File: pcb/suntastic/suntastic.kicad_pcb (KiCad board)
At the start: 2 copper layers, 105 parts, among them J1 Screw_Terminal_01x02, J2 Pololu U1V10F5, J3 Supercap IN, J4 FBB04004-F40S1003K6M, J5 Vin_TO_buck_boost, J6 Vout_FROM_buck_boost, J7 Conn_01x04_Pin, J8 Conn_01x04_Pin, J9 Conn_01x08_Pin, SW1 EVP-BF6C1A000, U1 TLV3691IDCKR, U2 REF35102QDBVR, U3 REF35409QDBVR, U4 TLV3691IDCKR, U5 TC7WH02FU_LJCT, U6 TPS22917DBV, U7 TPL5010, U8 XC6220B331MR

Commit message: Rework watchdog
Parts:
- removed TP10: IO1, TestPoint:TestPoint_Pad_D1.5mm
- removed TP11: IO6, TestPoint:TestPoint_Pad_D1.5mm
- removed TP12: IO8, TestPoint:TestPoint_Pad_D1.5mm
- removed TP13: IO7, TestPoint:TestPoint_Pad_D1.5mm
- removed TP14: VDD_nRF, TestPoint:TestPoint_Pad_D1.5mm
- removed TP6: IO4, TestPoint:TestPoint_Pad_D1.5mm
- removed TP7: IO2, TestPoint:TestPoint_Pad_D1.5mm
- removed TP8: IO5, TestPoint:TestPoint_Pad_D1.5mm
- removed TP9: IO3, TestPoint:TestPoint_Pad_D1.5mm
- added C21: 1uF, Capacitor_SMD:C_0603_1608Metric_Pad1.08x0.95mm_HandSolder, F.Cu at (56.7, 77.5)
- added C24: 0.1uF, Capacitor_SMD:C_0603_1608Metric_Pad1.08x0.95mm_HandSolder, F.Cu at (72.1, 71.4)
- added C25: 1uF, Capacitor_SMD:CP_Elec_4x4.5, F.Cu at (68.3, 73.7)
- added JP28: SolderJumper_2_Open, Jumper:SolderJumper-2_P1.3mm_Open_RoundedPad1.0x1.5mm, F.Cu at (59.3, 75.3)
- added R4: R, Resistor_SMD:R_0603_1608Metric_Pad0.98x0.95mm_HandSolder, F.Cu at (59.3, 83.5)
- added R7: R, Resistor_SMD:R_0603_1608Metric_Pad0.98x0.95mm_HandSolder, F.Cu at (59.3, 82.0)
- added R8: R, Resistor_SMD:R_0603_1608Metric_Pad0.98x0.95mm_HandSolder, F.Cu at (56.7, 81.0)
- added U10: TC7WH08FK_LJCT, Package_SO:TSSOP-8_3x3mm_P0.65mm, F.Cu at (74.9, 73.3)
- added U9: TPS22917DBV, Package_TO_SOT_SMD:SOT-23-6, F.Cu at (59.3, 79.0)
- JP27: value Jumper_2_Open -> SolderJumper_2_Open
- TP5: footprint TestPoint:TestPoint_Pad_D1.5mm -> TestPoint:TestPoint_Pad_D1.0mm
- U5: footprint Package_SO:Zetex_SM8 -> Package_SO:TSSOP-8_3x3mm_P0.65mm
- moved RV1 139.1 mm to (47.3, 72.6), turned to 180 degrees
- moved JP22 136.0 mm to (54.1, 79.7), turned to 180 degrees
- moved U7 134.6 mm to (53.7, 82.8)
- moved SW1 133.2 mm to (47.9, 80.0), turned to -90 degrees
- moved JP27 116.4 mm to (74.0, 83.0), turned to -90 degrees
- moved J1 85.6 mm to (130.0, 96.0)
- moved J2 85.4 mm to (141.7, 89.8)
- moved J9 32.4 mm to (174.6, 77.8), turned to 180 degrees
- moved JP20 28.9 mm to (144.6, 73.3), turned to -90 degrees
- moved JP25 28.5 mm to (149.6, 57.8)
- moved J8 27.7 mm to (150.8, 70.7)
- moved TP3 27.6 mm to (71.1, 83.9), turned to -90 degrees
- moved C18 22.2 mm to (166.3, 76.8)
- moved C17 22.0 mm to (159.8, 76.8), turned to 180 degrees
- moved TP4 21.7 mm to (163.1, 77.2)
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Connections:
- J9 pad 2: /WisBlock Core Module - RAK4631/IO2 -> /WisBlock Core Module - RAK4631/IO5
- J9 pad 4: /WisBlock Core Module - RAK4631/IO4 -> /WisBlock Core Module - RAK4631/IO6
- J9 pad 5: /WisBlock Core Module - RAK4631/IO5 -> /WisBlock Core Module - RAK4631/IO4
- J9 pad 6: /WisBlock Core Module - RAK4631/IO6 -> /WisBlock Core Module - RAK4631/IO2
- JP22 pad 1: 3.3V -> V_boost_uvlo
- JP27 pad 1: /Watchdog timer/RST_SIGNAL -> Net-(JP27-A)
- JP27 pad 2: nRF_RESET -> Net-(J1-Pin_1)
- SW1 pad 2: 3.3V -> V_boost_uvlo
- U6 pad 3: Net-(JP15-B) -> Net-(U10-OUT_2)
- U6 pad 5: unconnected-(U6-QOD-Pad5) -> Net-(JP27-A)
- U7 pad 4: unconnected-(U7-DONE-Pad4) -> Net-(JP28-A)
- U7 pad 5: unconnected-(U7-WAKE-Pad5) -> Net-(U7-WAKE)
- U7 pad 6: /Watchdog timer/RST_SIGNAL -> RST_SIGNAL
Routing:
- net V_boost_uvlo: track 19.9 -> 126.2 mm, vias 0 -> 4
- net V_supercap: track 0.00 -> 27.1 mm, vias 0 -> 2
- net /WisBlock Core Module - RAK4631/IO8: track 0.00 -> 20.4 mm
- net Net-(J3-Pin_2): track 0.00 -> 18.5 mm
- net /WisBlock Core Module - RAK4631/IO7: track 0.00 -> 16.9 mm
- net Net-(JP16-C): track 4.31 -> 21.0 mm
- net Net-(JP18-B): track 0.00 -> 14.6 mm
- net Net-(U7-DELAY/M_RST): track 0.00 -> 14.4 mm, vias 0 -> 2
- net Net-(JP28-A): track 0.00 -> 13.1 mm, vias 0 -> 2
- net /WisBlock Core Module - RAK4631/IO2: track 0.00 -> 12.6 mm
- net /WisBlock Core Module - RAK4631/IO1: track 0.00 -> 10.9 mm
- net /Sheetname: UVLO with latched output/RESET: track 12.9 -> 2.29 mm
- net /WisBlock Core Module - RAK4631/IO4: track 0.00 -> 10.5 mm
- net /WisBlock Core Module - RAK4631/IO3: track 0.00 -> 9.41 mm
- net /WisBlock Core Module - RAK4631/IO5: track 0.00 -> 9.02 mm
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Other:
- board text added: "Load Switch"
- board text added: "Supercapacitor"
- board text added: "Watchdog"

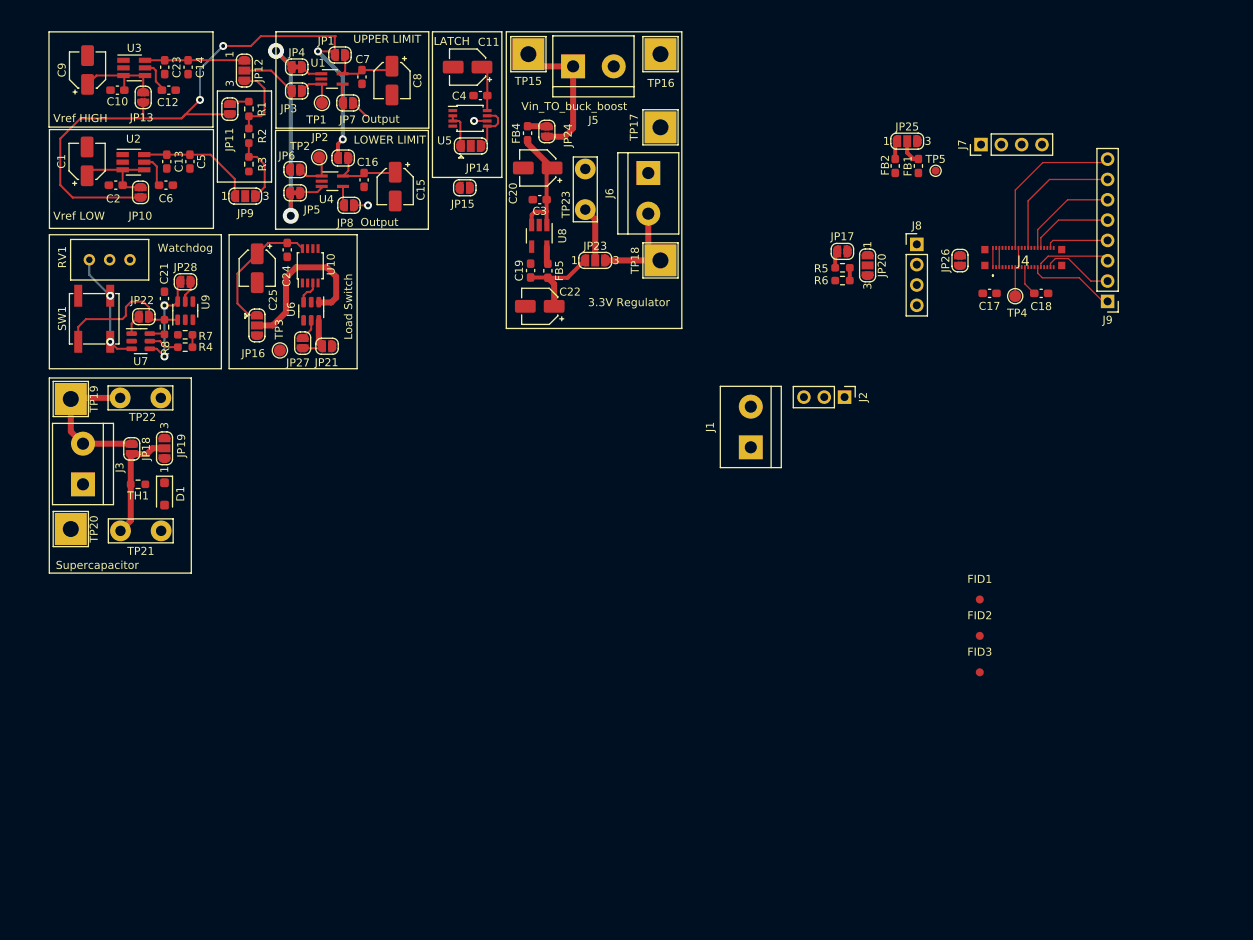
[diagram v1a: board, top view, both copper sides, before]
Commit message: Add screw terminals for external MPPT module and PV input
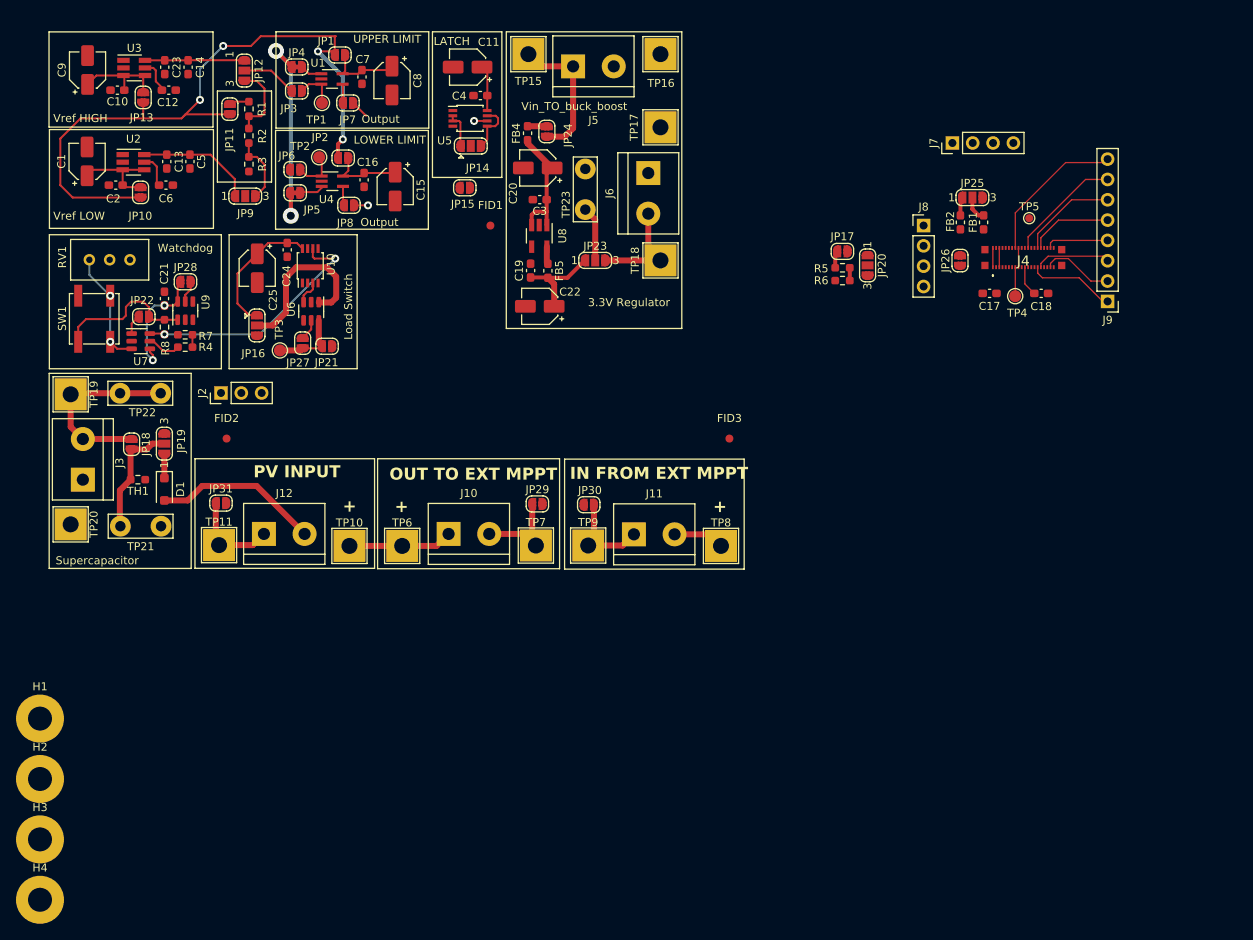
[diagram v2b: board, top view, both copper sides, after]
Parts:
- removed J1: Screw_Terminal_01x02, TerminalBlock:TerminalBlock_bornier-2_P5.08mm
- added H1: MountingHole, MountingHole:MountingHole_3mm_Pad, F.Cu at (41.1, 129.9)
- added H2: MountingHole, MountingHole:MountingHole_3mm_Pad, F.Cu at (41.1, 137.5)
- added H3: MountingHole, MountingHole:MountingHole_3mm_Pad, F.Cu at (41.1, 145.1)
- added H4: MountingHole, MountingHole:MountingHole_3mm_Pad, F.Cu at (41.1, 152.6)
- added J10: OUT TO EXT MPPT, TerminalBlock:TerminalBlock_bornier-2_P5.08mm, F.Cu at (92.2, 106.9)
- added J11: INPUT FROM EXT MPPT, TerminalBlock:TerminalBlock_bornier-2_P5.08mm, F.Cu at (115.4, 106.9)
- added J12: PV IN, TerminalBlock:TerminalBlock_bornier-2_P5.08mm, F.Cu at (69.1, 106.9)
- added JP29: Jumper_2_Open, Jumper:SolderJumper-2_P1.3mm_Open_RoundedPad1.0x1.5mm, F.Cu at (103.3, 103.1)
- added JP30: Jumper_2_Open, Jumper:SolderJumper-2_P1.3mm_Open_RoundedPad1.0x1.5mm, F.Cu at (109.7, 103.2)
- added JP31: Jumper_2_Open, Jumper:SolderJumper-2_P1.3mm_Open_RoundedPad1.0x1.5mm, F.Cu at (63.8, 103.0)
- added TP10: PV_VIN, TestPoint:TestPoint_THTPad_4.0x4.0mm_Drill2.0mm, F.Cu at (79.8, 108.4)
- added TP11: PV_GND, TestPoint:TestPoint_THTPad_4.0x4.0mm_Drill2.0mm, F.Cu at (63.5, 108.3)
- added TP6: PV_TO_MPPT, TestPoint:TestPoint_THTPad_4.0x4.0mm_Drill2.0mm, F.Cu at (86.4, 108.4)
- added TP7: GND_TO_MPPT, TestPoint:TestPoint_THTPad_4.0x4.0mm_Drill2.0mm, F.Cu at (103.1, 108.3)
- added TP8: OUT_FROM_MPPT, TestPoint:TestPoint_THTPad_4.0x4.0mm_Drill2.0mm, F.Cu at (126.3, 108.4)
- added TP9: GND_FROM_MPPT, TestPoint:TestPoint_THTPad_4.0x4.0mm_Drill2.0mm, F.Cu at (109.7, 108.3)
- R4: value R -> 1.8M
- R7: value R -> 3.3M
- moved FID2 97.3 mm to (64.5, 95.0)
- moved J2 77.9 mm to (63.8, 89.2), turned to 90 degrees
- moved FID1 77.0 mm to (97.5, 68.3)
- moved FID3 42.8 mm to (127.3, 95.0)
- moved TP5 13.1 mm to (164.8, 67.4)
- moved FB1 10.8 mm to (159.1, 67.9)
- moved JP25 10.8 mm to (157.7, 64.8)
- moved FB2 10.8 mm to (156.2, 67.9)
- moved J7 3.59 mm to (155.2, 58.0)
- moved J8 2.50 mm to (151.6, 68.3)
- moved J3 0.58 mm to (46.5, 100.1)
- moved TH1 0.58 mm to (53.4, 100.1)
- moved TP19 0.58 mm to (45.0, 89.4)
- moved TP20 0.58 mm to (45.0, 105.7)
- moved TP21 0.58 mm to (56.3, 105.9)
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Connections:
- D1 pad 2: PV_DIRECT_NO_MPPT -> PV_+
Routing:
- net PV_+: track 0.00 -> 33.8 mm
- net RST_SIGNAL: track 1.87 -> 31.1 mm, vias 0 -> 2
- net Net-(J10-Pin_2): track 0.00 -> 11.8 mm
- net Net-(J11-Pin_1): track 0.00 -> 11.7 mm
- net Net-(J12-Pin_1): track 0.00 -> 11.6 mm
- net MPPT_OUT: track 0.00 -> 6.40 mm
- net Net-(J3-Pin_2): track 18.5 -> 23.6 mm
- net Net-(D1-K): track 0.00 -> 3.00 mm
- net Net-(JP21-A): track 5.90 -> 8.85 mm
- net /WisBlock Core Module - RAK4631/IO7: track 16.9 -> 14.3 mm
- net Net-(JP28-A): track 13.1 -> 14.9 mm
- net /WisBlock Core Module - RAK4631/IO8: track 20.4 -> 18.7 mm
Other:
- board text added: "+"
- board text added: "IN FROM EXT MPPT"
- board text added: "OUT TO EXT MPPT"
- board text added: "PV INPUT"
